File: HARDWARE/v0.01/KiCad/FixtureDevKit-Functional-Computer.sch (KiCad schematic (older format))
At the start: 27 parts, among them J79 JST-2P-RA, J80 Conn_01x35, J81 USB_A, J82 CHIP4B2B, J83 VBUS, J84 Conn_01x35, J85 SF-352X-SMT, J86 Conn_01x20, J87 Conn_01x20, J88 CHIP4LH, J89 CHIP4RH, J90 Conn_01x20, J91 Conn_01x20, SW10 YSS-19-1202-N, SW11 TL9210AF260Q

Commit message: beginning pcb layout
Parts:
- J86, J87: footprint Pin_Headers:Pin_Header_Straight_1x20_Pitch2.54mm_SMD_Pin1Left -> Pin_Headers:Pin_Header_Straight_1x20_Pitch2.54mm
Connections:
- wire segments 197 -> 196
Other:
- moved on the sheet: F1, SW10
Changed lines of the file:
@@
 F 0 "J86" H 7750 2850 50  0000 C CNN
 F 1 "Conn_01x20" H 7750 750 50  0000 C CNN
-F 2 "Pin_Headers:Pin_Header_Straight_1x20_Pitch2.54mm_SMD_Pin1Left" H 7750 1850 50  0001 C CNN
+F 2 "Pin_Headers:Pin_Header_Straight_1x20_Pitch2.54mm" H 7750 1850 50  0001 C CNN
 F 3 "" H 7750 1850 50  0001 C CNN
 	1    7750 1850
@@
 F 0 "J87" H 7750 5550 50  0000 C CNN
 F 1 "Conn_01x20" H 7750 3450 50  0000 C CNN
-F 2 "Pin_Headers:Pin_Header_Straight_1x20_Pitch2.54mm_SMD_Pin1Left" H 7750 4550 50  0001 C CNN
+F 2 "Pin_Headers:Pin_Header_Straight_1x20_Pitch2.54mm" H 7750 4550 50  0001 C CNN
 F 3 "" H 7750 4550 50  0001 C CNN
 	1    7750 4550
@@
 $EndComp
 $Comp
-L GND #PWR055
+L GND #PWR061
 U 1 1 59EE7DE0
 P 7450 900
-F 0 "#PWR055" H 7450 650 50  0001 C CNN
+F 0 "#PWR061" H 7450 650 50  0001 C CNN
 F 1 "GND" H 7450 750 50  0000 C CNN
 F 2 "" H 7450 900 50  0001 C CNN
@@
 $EndComp
 $Comp
-L GND #PWR056
+L GND #PWR062
 U 1 1 59EE7F13
 P 9800 900
-F 0 "#PWR056" H 9800 650 50  0001 C CNN
+F 0 "#PWR062" H 9800 650 50  0001 C CNN
 F 1 "GND" H 9800 750 50  0000 C CNN
 F 2 "" H 9800 900 50  0001 C CNN
@@
 $EndComp
 $Comp
-L GND #PWR057
+L GND #PWR063
 U 1 1 59EE8282
 P 7450 3600
-F 0 "#PWR057" H 7450 3350 50  0001 C CNN
+F 0 "#PWR063" H 7450 3350 50  0001 C CNN
 F 1 "GND" H 7450 3450 50  0000 C CNN
 F 2 "" H 7450 3600 50  0001 C CNN
@@
 $EndComp
 $Comp
-L GND #PWR058
+L GND #PWR064
 U 1 1 59EE829F
 P 9800 3600
-F 0 "#PWR058" H 9800 3350 50  0001 C CNN
+F 0 "#PWR064" H 9800 3350 50  0001 C CNN
 F 1 "GND" H 9800 3450 50  0000 C CNN
 F 2 "" H 9800 3600 50  0001 C CNN
@@
 $EndComp
 $Comp
-L GND #PWR059
+L GND #PWR065
 U 1 1 59EE95A1
 P 1900 7450
-F 0 "#PWR059" H 1900 7200 50  0001 C CNN
+F 0 "#PWR065" H 1900 7200 50  0001 C CNN
 F 1 "GND" H 1900 7300 50  0000 C CNN
 F 2 "" H 1900 7450 50  0001 C CNN
@@
 $EndComp
 $Comp
-L GND #PWR060
+L GND #PWR066
 U 1 1 59EEA1C1
 P 900 7450
-F 0 "#PWR060" H 900 7200 50  0001 C CNN
+F 0 "#PWR066" H 900 7200 50  0001 C CNN
 F 1 "GND" H 900 7300 50  0000 C CNN
 F 2 "" H 900 7450 50  0001 C CNN
@@
 $EndComp
 $Comp
-L GND #PWR061
+L GND #PWR067
 U 1 1 59EEADAD
 P 2650 7250
-F 0 "#PWR061" H 2650 7000 50  0001 C CNN
+F 0 "#PWR067" H 2650 7000 50  0001 C CNN
 F 1 "GND" H 2650 7100 50  0000 C CNN
 F 2 "" H 2650 7250 50  0001 C CNN
@@
 BAT
 $Comp
-L GND #PWR062
+L GND #PWR068
 U 1 1 59EEB6E8
 P 3150 6650
-F 0 "#PWR062" H 3150 6400 50  0001 C CNN
+F 0 "#PWR068" H 3150 6400 50  0001 C CNN
 F 1 "GND" H 3150 6500 50  0000 C CNN
 F 2 "" H 3150 6650 50  0001 C CNN
@@
 USBOTG_B_ID
 $Comp
-L GND #PWR063
+L GND #PWR069
 U 1 1 59EF55B6
 P 3600 7300
-F 0 "#PWR063" H 3600 7050 50  0001 C CNN
+F 0 "#PWR069" H 3600 7050 50  0001 C CNN
 F 1 "GND" H 3600 7150 50  0000 C CNN
 F 2 "" H 3600 7300 50  0001 C CNN
@@
 $EndComp
 $Comp
-L GND #PWR064
+L GND #PWR070
 U 1 1 59EF61DC
 P 4450 7600
-F 0 "#PWR064" H 4450 7350 50  0001 C CNN
+F 0 "#PWR070" H 4450 7350 50  0001 C CNN
 F 1 "GND" H 4450 7450 50  0000 C CNN
 F 2 "" H 4450 7600 50  0001 C CNN
@@
 $EndComp
 $Comp
-L GND #PWR065
+L GND #PWR071
 U 1 1 59F0E393
 P 5750 7650
-F 0 "#PWR065" H 5750 7400 50  0001 C CNN
+F 0 "#PWR071" H 5750 7400 50  0001 C CNN
 F 1 "GND" H 5750 7500 50  0000 C CNN
 F 2 "" H 5750 7650 50  0001 C CNN
@@
 Sheet Connections
 $Comp
-L +5V #PWR066
+L +5V #PWR072
 U 1 1 59F1E155
 P 1500 1350
-F 0 "#PWR066" H 1500 1200 50  0001 C CNN
+F 0 "#PWR072" H 1500 1200 50  0001 C CNN
 F 1 "+5V" H 1500 1490 50  0000 C CNN
 F 2 "" H 1500 1350 50  0001 C CNN
@@
 +5V
 $Comp
-L +5V #PWR067
+L +5V #PWR073
 U 1 1 59F1EC3F
 P 800 4800
-F 0 "#PWR067" H 800 4650 50  0001 C CNN
+F 0 "#PWR073" H 800 4650 50  0001 C CNN
 F 1 "+5V" H 800 4940 50  0000 C CNN
 F 2 "" H 800 4800 50  0001 C CNN
@@
 L Fuse F1
 U 1 1 59F1EC7A
+P 700 5400
+F 0 "F1" V 780 5400 50  0000 C CNN
+F 1 "1206SFP300F" V 625 5400 50  0000 C CNN
+F 2 "Fuse_Holders_and_Fuses:Fuse_SMD1206_HandSoldering" V 630 5400 50  0001 C CNN
+F 3 "" H 700 5400 50  0001 C CNN
+	1    700  5400
+	1    0    0    -1
+$EndComp
+$Comp
+L SW_Push_SPDT SW10
+U 1 1 59F1EDC7
 P 800 5000
-F 0 "F1" V 880 5000 50  0000 C CNN
-F 1 "1206SFP300F" V 725 5000 50  0000 C CNN
-F 2 "Fuse_Holders_and_Fuses:Fuse_SMD1206_HandSoldering" V 730 5000 50  0001 C CNN
+F 0 "SW10" H 800 5170 50  0000 C CNN
+F 1 "YSS-19-1202-N" H 800 4800 50  0000 C CNN
+F 2 "" H 800 5000 50  0001 C CNN
 F 3 "" H 800 5000 50  0001 C CNN
 	1    800  5000
-	1    0    0    -1
-$EndComp
-$Comp
-L SW_Push_SPDT SW10
-U 1 1 59F1EDC7
-P 800 5400
-F 0 "SW10" H 800 5570 50  0000 C CNN
-F 1 "YSS-19-1202-N" H 800 5200 50  0000 C CNN
-F 2 "" H 800 5400 50  0001 C CNN
-F 3 "" H 800 5400 50  0001 C CNN
-	1    800  5400
 	0    1    1    0
 $EndComp
-NoConn ~ 900  5600
+NoConn ~ 900  5200
 Text Label 700  6000 0    60   ~ 0
 C4-PWR-IN
@@
 	3150 1700 3450 1700
 Wire Wire Line
-	3450 1800 3150 1800
+	3150 1800 3450 1800
 Wire Wire Line
 	3150 1900 3450 1900
@@
 	3150 4700 3450 4700
 Wire Wire Line
-	3150 4800 3450 4800
-Wire Wire Line
-	3150 4900 3450 4900
-Wire Wire Line
-	3150 5000 3450 5000
+	3450 4800 3150 4800
+Wire Wire Line
+	3450 4900 3150 4900
+Wire Wire Line
+	3450 5000 3150 5000
 Wire Wire Line
 	5400 5000 5100 5000
@@
 	5400 1800 5100 1800
 Wire Wire Line
-	5100 1700 5400 1700
+	5400 1700 5100 1700
 Wire Wire Line
 	5400 1600 5100 1600
@@
 Connection ~ 3150 1600
 Wire Wire Line
-	3150 4600 3150 5000
+	3150 5000 3150 4600
 Connection ~ 3150 4700
 Connection ~ 3150 4800
@@
 Connection ~ 5400 4900
 Wire Wire Line
-	5400 4600 5400 5000
-Wire Wire Line
-	5400 1600 5400 1900
+	5400 4600 5400 5250
+Wire Wire Line
+	5400 1500 5400 1900
 Connection ~ 5400 1800
 Connection ~ 5400 1700
@@
 	1250 1350 1500 1350
 Wire Wire Line
-	800  4800 800  4850
-Wire Wire Line
-	800  5150 800  5200
-Wire Wire Line
-	700  6000 700  5600
+	700  5550 700  6000
 Wire Notes Line
 	500  4250 1300 4250
@@
 Wire Notes Line
 	500  750  2200 750
+$Comp
+L GND #PWR074
+U 1 1 59F28C8B
+P 5400 1500
+F 0 "#PWR074" H 5400 1250 50  0001 C CNN
+F 1 "GND" H 5400 1350 50  0000 C CNN
+F 2 "" H 5400 1500 50  0001 C CNN
+F 3 "" H 5400 1500 50  0001 C CNN
+	1    5400 1500
+	-1   0    0    1
+$EndComp
+Connection ~ 5400 1600
+$Comp
+L GND #PWR075
+U 1 1 59F28EDE
+P 5400 5250
+F 0 "#PWR075" H 5400 5000 50  0001 C CNN
+F 1 "GND" H 5400 5100 50  0000 C CNN
+F 2 "" H 5400 5250 50  0001 C CNN
+F 3 "" H 5400 5250 50  0001 C CNN
+	1    5400 5250
+	1    0    0    -1
+$EndComp
+Connection ~ 5400 5000
+Wire Wire Line
+	700  5200 700  5250
 $EndSCHEMATC

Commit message: pcb roughly 15cm x 15cm
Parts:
- J89: footprint Pin_Headers:Pin_Header_Straight_2x19_Pitch2.54mm -> Pin_Headers:Pin_Header_Straight_2x20_Pitch2.54mm
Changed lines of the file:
@@
 F 0 "J89" H 8150 4950 60  0000 C CNN
 F 1 "CHIP4RH" H 8400 2800 60  0000 C CNN
-F 2 "Pin_Headers:Pin_Header_Straight_2x19_Pitch2.54mm" H 8700 2900 60  0001 C CNN
+F 2 "Pin_Headers:Pin_Header_Straight_2x20_Pitch2.54mm" H 8700 2900 60  0001 C CNN
 F 3 "" H 8700 2900 60  0001 C CNN
 	1    8650 2900

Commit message: adding datasheets and laying out PCB
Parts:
- removed J81: USB_A, symbol USB_A
- removed TP103: D-, TestPoint:TestPoint, symbol TEST
- removed TP104: D+, TestPoint:TestPoint, symbol TEST
- added P2: USB-A1HSW6, USB-A1HSW6:OST_USB-A1HSW6, symbol USB-A1HSW6
- F1: footprint Fuse_Holders_and_Fuses:Fuse_SMD1206_HandSoldering -> 1206:1206
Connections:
- wire segments 196 -> 194
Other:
- moved on the sheet: J83, JP1
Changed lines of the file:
@@
 LIBS:valves
 LIBS:TCA6424ARGJR
+LIBS:USB-A1HSW6
 LIBS:Fixture-Dev-Kit-cache
 EELAYER 25 0
@@
 Text Label 5500 4100 0    60   ~ 0
 USBOTG_B_DP
-Text Label 4050 6900 0    60   ~ 0
+Text Label 4000 6750 2    60   ~ 0
 USBOTG_B_DM
-Text Label 3950 7600 2    60   ~ 0
+Text Label 4000 7650 2    60   ~ 0
 USBOTG_B_ID
 $Comp
 L GND #PWR069
 U 1 1 59EF55B6
-P 3600 7300
-F 0 "#PWR069" H 3600 7050 50  0001 C CNN
-F 1 "GND" H 3600 7150 50  0000 C CNN
-F 2 "" H 3600 7300 50  0001 C CNN
-F 3 "" H 3600 7300 50  0001 C CNN
-	1    3600 7300
+P 3950 7100
+F 0 "#PWR069" H 3950 6850 50  0001 C CNN
+F 1 "GND" H 3950 6950 50  0000 C CNN
+F 2 "" H 3950 7100 50  0001 C CNN
+F 3 "" H 3950 7100 50  0001 C CNN
+	1    3950 7100
 	1    0    0    -1
 $EndComp
@@
 L Jumper_NC_Small JP1
 U 1 1 59EF5E24
-P 4200 7600
-F 0 "JP1" H 4200 7680 50  0000 C CNN
-F 1 "Jumper_NC" H 4210 7540 50  0000 C CNN
-F 2 "Pin_Headers:Pin_Header_Straight_1x02_Pitch2.54mm" H 4200 7600 50  0001 C CNN
-F 3 "" H 4200 7600 50  0001 C CNN
-	1    4200 7600
+P 4250 7650
+F 0 "JP1" H 4250 7730 50  0000 C CNN
+F 1 "Jumper_NC" H 4260 7590 50  0000 C CNN
+F 2 "Pin_Headers:Pin_Header_Straight_1x02_Pitch2.54mm" H 4250 7650 50  0001 C CNN
+F 3 "" H 4250 7650 50  0001 C CNN
+	1    4250 7650
 	1    0    0    -1
 $EndComp
@@
 L GND #PWR070
 U 1 1 59EF61DC
-P 4450 7600
-F 0 "#PWR070" H 4450 7350 50  0001 C CNN
-F 1 "GND" H 4450 7450 50  0000 C CNN
-F 2 "" H 4450 7600 50  0001 C CNN
-F 3 "" H 4450 7600 50  0001 C CNN
-	1    4450 7600
+P 4500 7650
+F 0 "#PWR070" H 4500 7400 50  0001 C CNN
+F 1 "GND" H 4500 7500 50  0000 C CNN
+F 2 "" H 4500 7650 50  0001 C CNN
+F 3 "" H 4500 7650 50  0001 C CNN
+	1    4500 7650
 	-1   0    0    1
 $EndComp
 Text Notes 3550 6250 0    98   ~ 0
 B2B USB-A
-Text Label 4050 6800 0    60   ~ 0
+Text Label 4000 6850 2    60   ~ 0
 USBOTG_B_DP
-$Comp
-L USB_A J81
-U 1 1 59EF4A5C
-P 3600 6800
-F 0 "J81" H 3400 7250 50  0000 L CNN
-F 1 "USB_A" H 3400 7150 50  0000 L CNN
-F 2 "" H 3750 6750 50  0001 C CNN
-F 3 "" H 3750 6750 50  0001 C CNN
-	1    3600 6800
-	1    0    0    -1
-$EndComp
 $Comp
 L Conn_01x02 J83
 U 1 1 59F0CB92
-P 4250 6500
-F 0 "J83" H 4250 6600 50  0000 C CNN
-F 1 "VBUS" V 4350 6450 50  0000 C CNN
-F 2 "Pin_Headers:Pin_Header_Straight_1x02_Pitch2.54mm" H 4250 6500 50  0001 C CNN
-F 3 "" H 4250 6500 50  0001 C CNN
-	1    4250 6500
-	1    0    0    -1
+P 3650 6550
+F 0 "J83" H 3650 6650 50  0000 C CNN
+F 1 "VBUS" V 3750 6500 50  0000 C CNN
+F 2 "Pin_Headers:Pin_Header_Straight_1x02_Pitch2.54mm" H 3650 6550 50  0001 C CNN
+F 3 "" H 3650 6550 50  0001 C CNN
+	1    3650 6550
+	-1   0    0    1
 $EndComp
 $Comp
@@
 F 0 "F1" V 780 5400 50  0000 C CNN
 F 1 "1206SFP300F" V 625 5400 50  0000 C CNN
-F 2 "Fuse_Holders_and_Fuses:Fuse_SMD1206_HandSoldering" V 630 5400 50  0001 C CNN
+F 2 "1206:1206" V 630 5400 50  0001 C CNN
 F 3 "" H 700 5400 50  0001 C CNN
 	1    700  5400
@@
 Text Label 3400 5300 2    60   ~ 0
 C4-PWR-IN
-$Comp
-L TEST TP104
-U 1 1 59F2229B
-P 4000 7100
-F 0 "TP104" H 4000 7400 50  0000 C BNN
-F 1 "D+" H 4000 7350 50  0000 C CNN
-F 2 "TestPoint:TestPoint" H 4000 7100 50  0001 C CNN
-F 3 "" H 4000 7100 50  0001 C CNN
-	1    4000 7100
-	0    1    1    0
-$EndComp
-$Comp
-L TEST TP103
-U 1 1 59F223B8
-P 3950 7200
-F 0 "TP103" H 3950 7500 50  0000 C BNN
-F 1 "D-" H 3950 7450 50  0000 C CNN
-F 2 "TestPoint:TestPoint" H 3950 7200 50  0001 C CNN
-F 3 "" H 3950 7200 50  0001 C CNN
-	1    3950 7200
-	0    1    1    0
-$EndComp
 Text Label 9900 3650 0    60   ~ 0
 C4-PWR-IN
@@
 Connection ~ 5400 2200
 Connection ~ 5400 2100
-Wire Wire Line
-	3900 6800 4050 6800
-Wire Wire Line
-	3900 6900 4050 6900
 Connection ~ 5400 4300
 Connection ~ 5400 4200
 Connection ~ 5400 4100
 Wire Wire Line
-	3500 7200 3600 7200
-Wire Wire Line
-	3600 7200 3600 7300
-Wire Wire Line
-	4450 7600 4300 7600
-Wire Wire Line
-	4100 7600 3950 7600
+	4500 7650 4350 7650
+Wire Wire Line
+	4150 7650 4000 7650
 Wire Notes Line
 	3300 6300 4700 6300
@@
 Wire Notes Line
 	3300 6100 4700 6100
-Wire Wire Line
-	3900 6600 4050 6600
-Wire Wire Line
-	4050 6600 4050 6500
 Wire Wire Line
 	4850 7200 4850 7250
@@
 Connection ~ 3450 4800
 Connection ~ 3450 4700
-Wire Wire Line
-	4000 7100 4000 6800
-Connection ~ 4000 6800
-Wire Wire Line
-	3950 7200 3950 6900
-Connection ~ 3950 6900
 Connection ~ 9700 950
 Text HLabel 1200 1550 0    60   Output ~ 0
@@
 Wire Wire Line
 	700  5200 700  5250
+$Comp
+L USB-A1HSW6 P2
+U 1 1 59F3E629
+P 4350 6850
+F 0 "P2" H 4250 7301 50  0000 L BNN
+F 1 "USB-A1HSW6" H 4250 6449 50  0000 L BNN
+F 2 "USB-A1HSW6:OST_USB-A1HSW6" H 4350 6850 50  0001 L BNN
+F 3 "On Shore Technology" H 4350 6850 50  0001 L BNN
+F 4 "None" H 4350 6850 50  0001 L BNN "Package"
+F 5 "Conn Usb Type a r/a White" H 4350 6850 50  0001 L BNN "Description"
+F 6 "Good" H 4350 6850 50  0001 L BNN "Availability"
+F 7 "USB-A1HSW6" H 4350 6850 50  0001 L BNN "MP"
+F 8 "0.31 USD" H 4350 6850 50  0001 L BNN "Price"
+	1    4350 6850
+	1    0    0    -1
+$EndComp
+Wire Wire Line
+	3850 6450 3850 6650
+Wire Wire Line
+	3850 6650 4150 6650
+Connection ~ 3850 6550
+Wire Wire Line
+	4150 6750 4000 6750
+Wire Wire Line
+	4150 6850 4000 6850
+Wire Wire Line
+	4150 6950 3950 6950
+Wire Wire Line
+	3950 6950 3950 7100
 $EndSCHEMATC

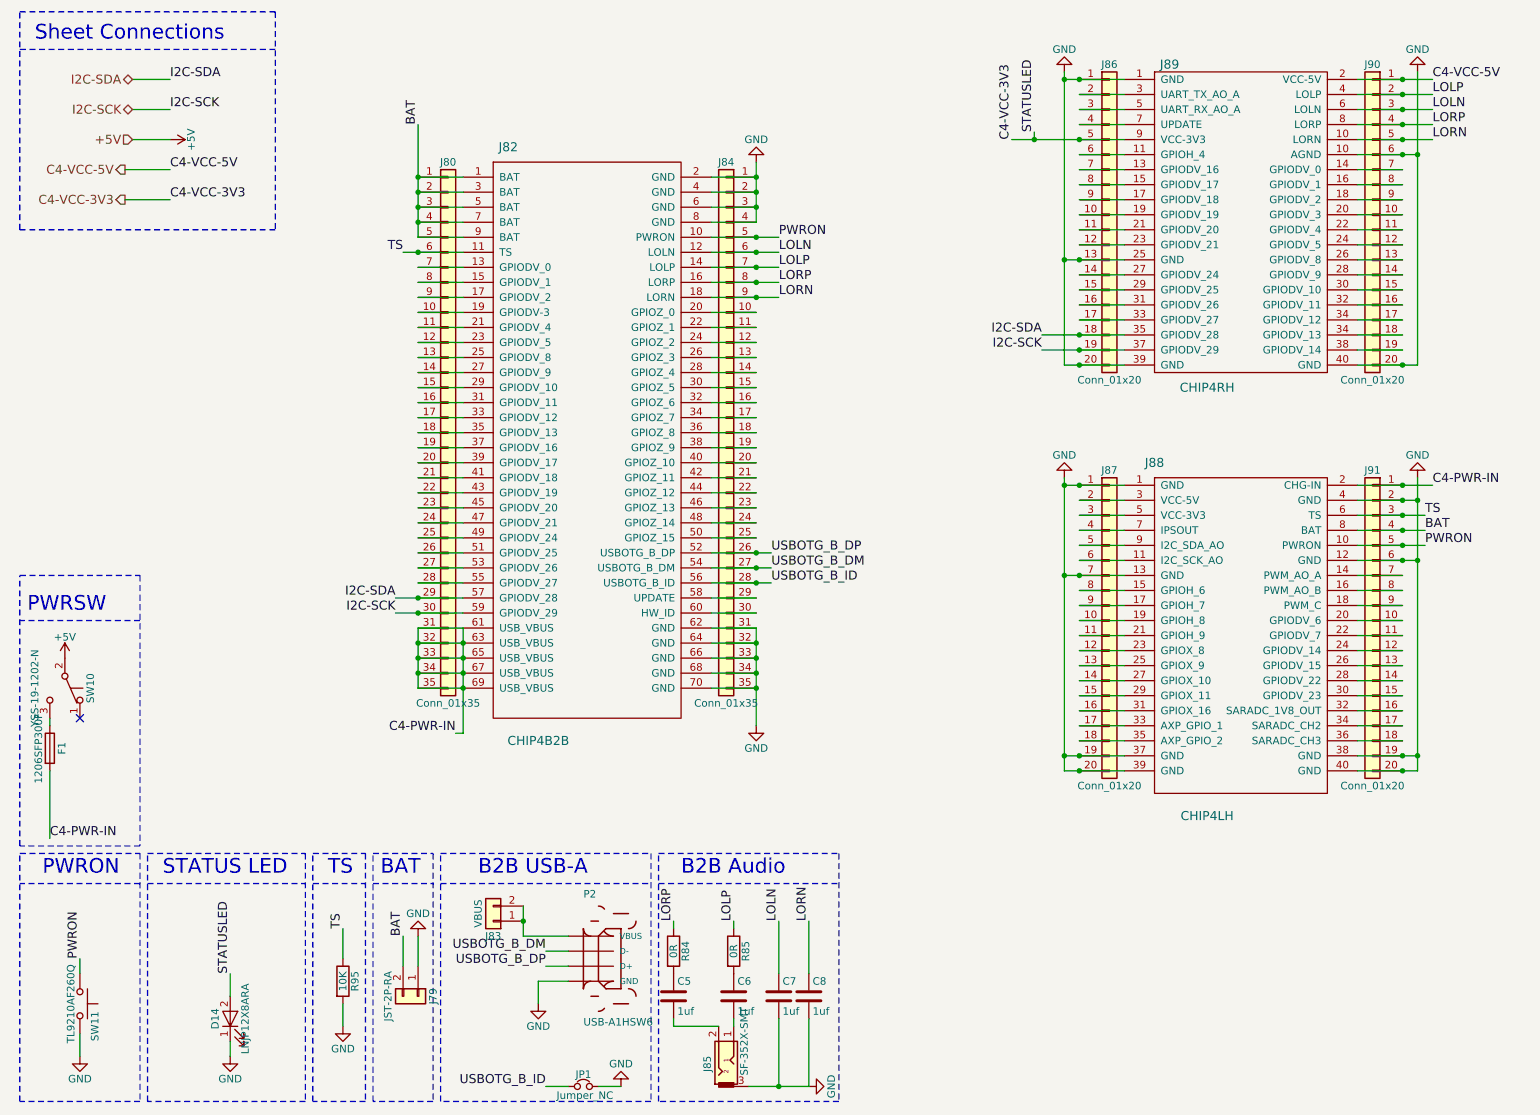
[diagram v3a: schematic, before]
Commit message: quasi-redoing entire schematic and layout
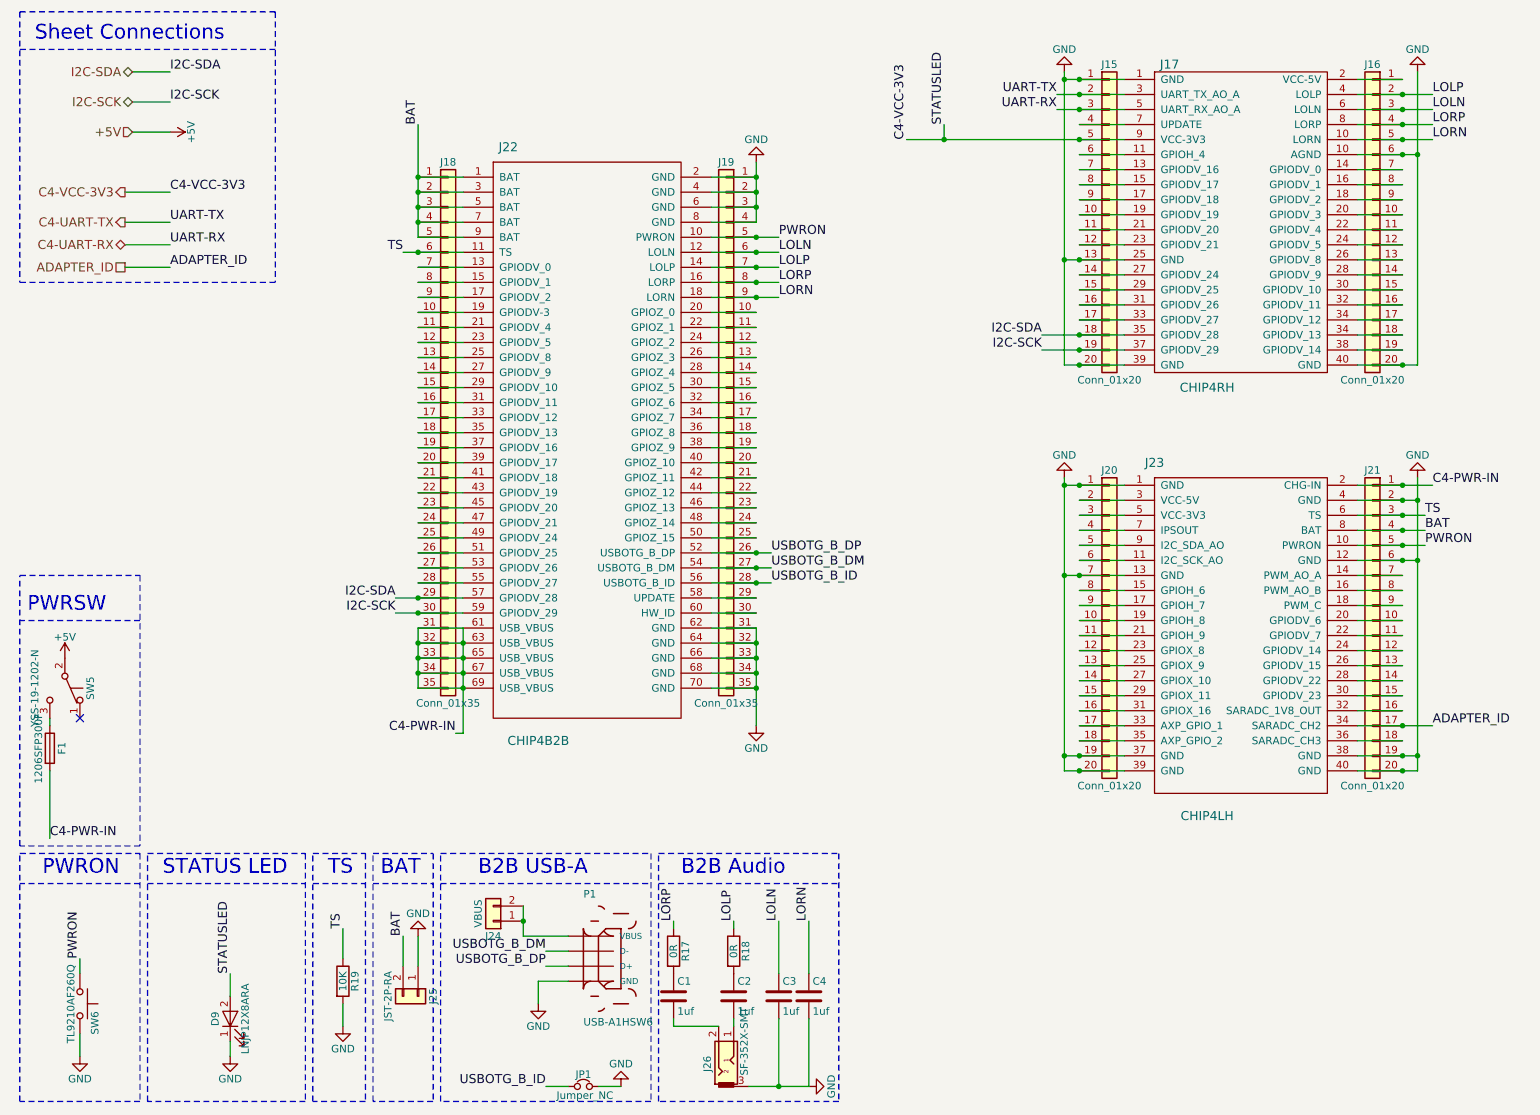
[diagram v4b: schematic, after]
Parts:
- renumbered C5 to C1, C6 to C2, C7 to C3, C8 to C4, D14 to D9, J86 to J15, J90 to J16, J89 to J17, J80 to J18, J84 to J19, J87 to J20, J91 to J21, J82 to J22, J88 to J23, J83 to J24, J79 to J25, J85 to J26, P2 to P1, R84 to R17, R85 to R18, R95 to R19, SW10 to SW5, SW11 to SW6
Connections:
- net ADAPTER_ID: now reaches J21.17 (Pin_17), J23.34 (SARADC_CH2)
- net C4-UART-TX: now reaches J15.2 (Pin_2), J17.3 (UART_TX_AO_A)
- net C4-UART-RX: now reaches J15.3 (Pin_3), J17.5 (UART_RX_AO_A)
- net C4-VCC-5V: no longer names the net of J16.1 (Pin_1), J17.2 (VCC-5V)

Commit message: updating layout
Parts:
- removed C1, C2, C3, C4: 1uf, Capacitors_SMD:C_0805_HandSoldering, symbol C
- removed J18, J19: Conn_01x35, Pin_Headers:Pin_Header_Straight_1x35_Pitch2.54mm, symbol Conn_01x35
- removed J22: CHIP4B2B, symbol CHIP4B2B
- removed J24: VBUS, Pin_Headers:Pin_Header_Straight_1x02_Pitch2.54mm, symbol Conn_01x02
- removed J26: SF-352X-SMT, symbol Audio-Jack-3
- removed JP1: Jumper_NC, Pin_Headers:Pin_Header_Straight_1x02_Pitch2.54mm, symbol Jumper_NC_Small
- removed P1: USB-A1HSW6, USB-A1HSW6:OST_USB-A1HSW6, symbol USB-A1HSW6
- removed R17, R18: 0R, Resistors_SMD:R_0805_HandSoldering, symbol R
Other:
- note removed: "B2B Audio\n"
- note removed: "B2B USB-A"

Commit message: updating layout footprints and board outline
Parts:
- SW5: footprint (none) -> YSS-19-1202-N:YSS-19-1202-N
- SW6: footprint (none) -> TL9210AF260Q:TL9210AF260Q
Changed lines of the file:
@@
 F 0 "SW6" H 950 7200 50  0000 L CNN
 F 1 "TL9210AF260Q" H 900 7040 50  0000 C CNN
-F 2 "" H 900 7300 50  0001 C CNN
+F 2 "TL9210AF260Q:TL9210AF260Q" H 900 7300 50  0001 C CNN
 F 3 "" H 900 7300 50  0001 C CNN
 	1    900  7100
@@
 F 0 "SW5" H 800 5170 50  0000 C CNN
 F 1 "YSS-19-1202-N" H 800 4800 50  0000 C CNN
-F 2 "" H 800 5000 50  0001 C CNN
+F 2 "YSS-19-1202-N:YSS-19-1202-N" H 800 5000 50  0001 C CNN
 F 3 "" H 800 5000 50  0001 C CNN
 	1    800  5000
